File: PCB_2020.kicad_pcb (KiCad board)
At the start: 2 copper layers, 109.5 x 87.9 mm, 34 parts, among them Q1 100V/17A, Q2 100V/17A, Q3 100V/17A, Q4 100V/17A, Q5 100V/17A, Q6 100V/17A, U1 AMP_DUE_SCH, U2 TL084CN, U3 DRV8874, U4 LoRa

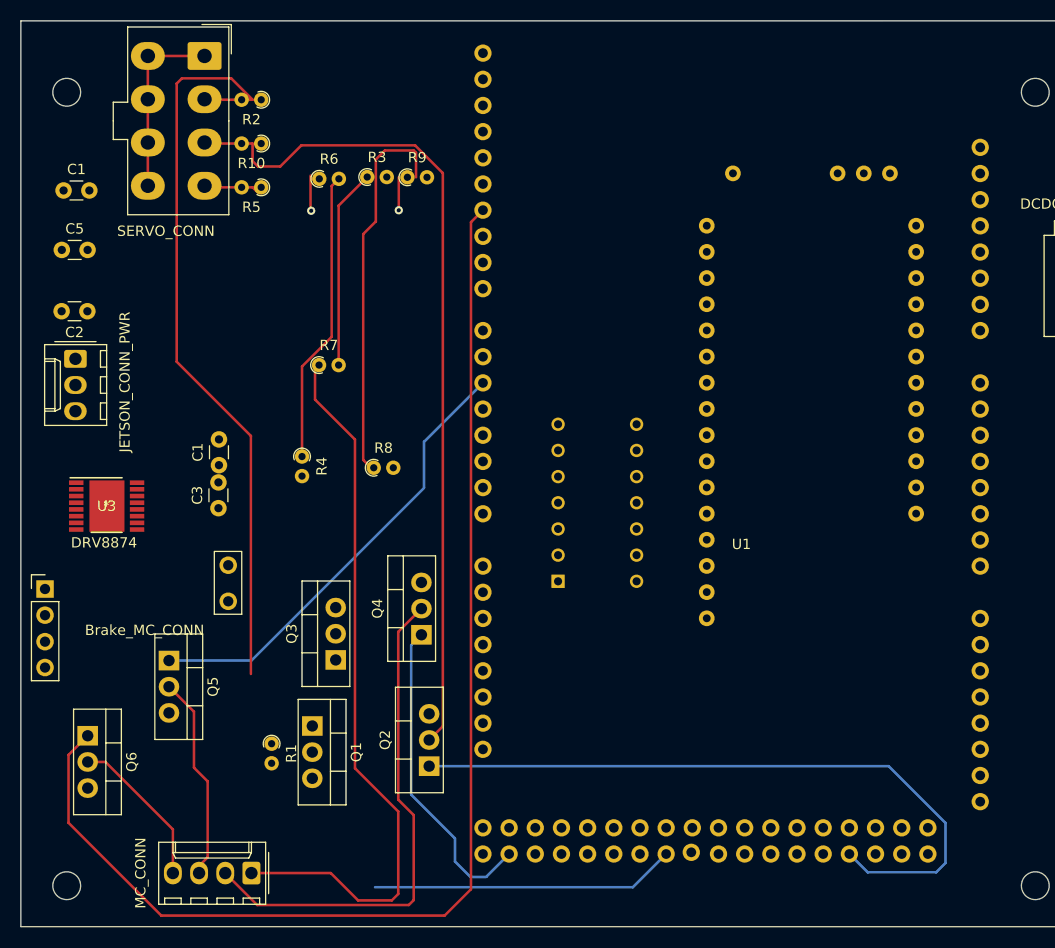
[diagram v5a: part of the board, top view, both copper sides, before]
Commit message: Added AND gate for Feather LoRa, and changed over to through hole components
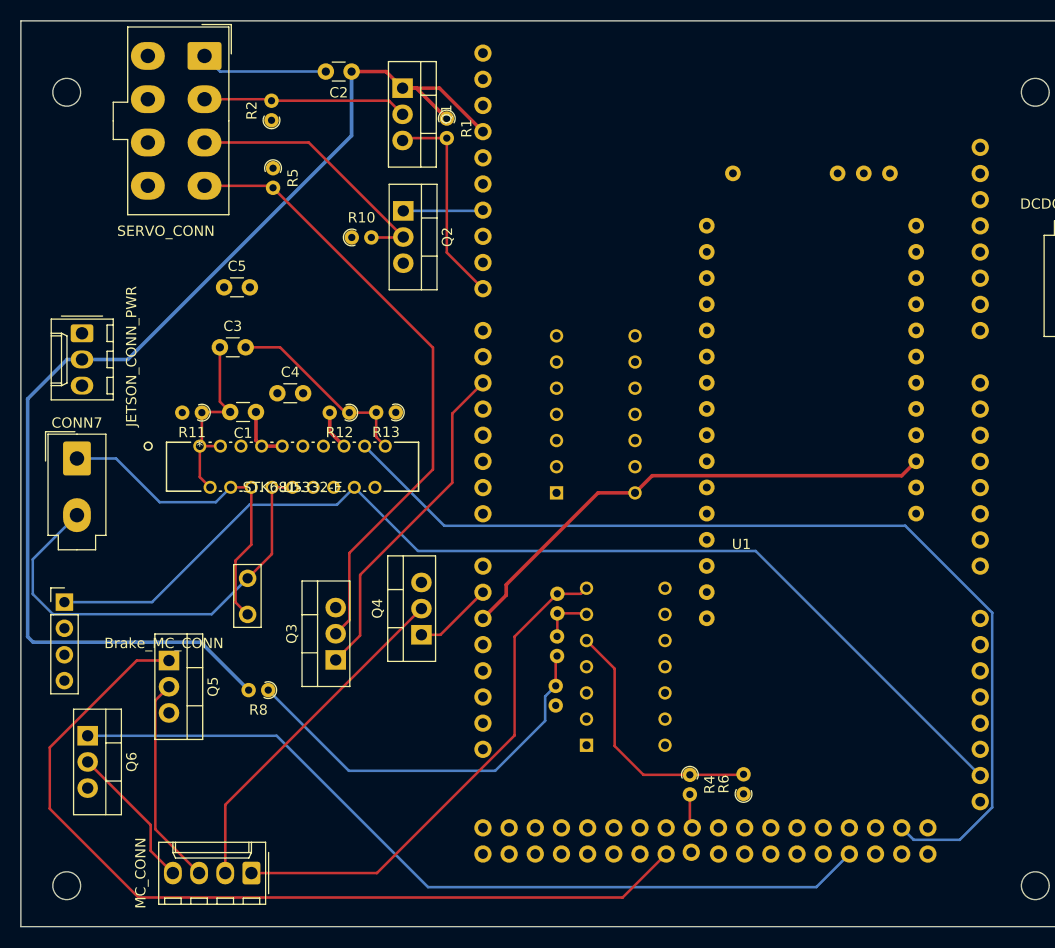
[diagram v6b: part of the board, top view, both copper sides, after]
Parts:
- removed the C1 at (131.0, 66.1)
- removed the C1 at (146.1, 92.8)
- added C1: 47u, Capacitor_THT:C_Disc_D3.0mm_W1.6mm_P2.50mm, F.Cu at (149.7, 87.6)
- added C4: 10u, Capacitor_THT:C_Disc_D3.0mm_W1.6mm_P2.50mm, F.Cu at (151.8, 85.8)
- added CONN7: Brake_CONN, Connector_Molex:Molex_Mini-Fit_Jr_5566-02A_2x01_P4.20mm_Vertical, F.Cu at (132.3, 92.1)
- added R11: R-Device, Resistor_THT:R_Axial_DIN0204_L3.6mm_D1.6mm_P1.90mm_Vertical, F.Cu at (144.4, 87.7)
- added R12: 4k, Resistor_THT:R_Axial_DIN0204_L3.6mm_D1.6mm_P1.90mm_Vertical, F.Cu at (158.8, 87.7)
- added R13: 1k, Resistor_THT:R_Axial_DIN0204_L3.6mm_D1.6mm_P1.90mm_Vertical, F.Cu at (163.3, 87.7)
- added U5: STK681-332-E, Drivetrain_control:STK681-332-E, F.Cu at (144.2, 90.9)
- C3: value 0.022uF -> 0.1u
- R3, R7, R9: moved to B.Cu
- U3: value DRV8874 -> SN74AS08N; footprint Drivetrain_control:DRV8874PWPR -> Drivetrain_control:SN74AS08N; moved to B.Cu
- moved R6 72.5 mm to (197.0, 124.7), turned to 90 degrees
- moved R1 63.0 mm to (168.2, 59.1)
- moved Q1 62.5 mm to (163.9, 56.2)
- moved Q2 53.9 mm to (164.0, 68.1), turned to 270 degrees
- moved U3 53.9 mm to (186.5, 80.2)
- moved R9 53.2 mm to (178.8, 116.1), turned to 90 degrees
- moved R4 48.7 mm to (191.8, 122.8)
- moved R3 48.2 mm to (178.9, 109.4), turned to 270 degrees
- moved C2 34.6 mm to (159.0, 54.6)
- moved R7 32.1 mm to (178.9, 105.3), turned to 270 degrees
- moved R8 23.9 mm to (150.9, 114.6), turned to 180 degrees
- moved C5 16.2 mm to (146.6, 75.5)
- moved U2 16.1 mm to (189.4, 104.7)
- moved C3 15.6 mm to (146.2, 81.3), turned to 0 degrees
- moved R10 12.7 mm to (159.0, 70.7), turned to 0 degrees
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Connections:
- C3 pad 1: +12V -> Net-(C1-Pad2)
- U1 pad 18: Brake_PWM_1 -> Net-(U1-Pad18)
- U1 pad 19: Brake_PWM_2 -> Net-(U1-Pad19)
- U1 pad 20: STEERING -> Net-(U1-Pad20)
- U1 pad 23: Net-(U1-Pad23) -> Brake_PWM_1
- U1 pad 26: Net-(U1-Pad26) -> Brake_PWM_2
- U1 pad 46: INPUT_A+_CTL -> FS1_CTL
- U1 pad 53: EN+_CTL -> FWD_CTL
- U1 pad 59: REV_CTL -> KS1_CTL
- U1 pad 67: KS1_CTL -> REV_CTL
- U1 pad 74: FWD_CTL -> EN+_CTL
- U1 pad 77: Net-(U1-Pad77) -> STEERING
- U1 pad 80: FS1_CTL -> INPUT_A+_CTL
- U3 pad 1: Brake_PWM_1 -> Net-(U3-Pad1)
- U3 pad 10: /LAUNCHXL-F28379D Breakout/Brake_Out_2 -> Net-(U3-Pad10)
- U3 pad 11: +12V -> Net-(U3-Pad11)
- U3 pad 12: Net-(C3-Pad2) -> Net-(U3-Pad12)
- U3 pad 14: Net-(C1-Pad2) -> +5V
- U3 pad 2: Brake_PWM_2 -> Net-(U3-Pad2)
- U3 pad 3: +3V3 -> Net-(U3-Pad3)
- U3 pad 5: +3V3 -> Net-(U3-Pad5)
- U3 pad 6: GND -> Net-(U3-Pad6)
- U3 pad 8: /LAUNCHXL-F28379D Breakout/Brake_Out_1 -> Net-(U3-Pad8)
- U3 pad 9: GND -> Net-(U3-Pad9)
- U4 pad 48: +3V3 -> Net-(U4-Pad48)
- U4 pad 55: Net-(U4-Pad55) -> +5V
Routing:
- net +3V3: track 0.00 -> 115.6 mm
- net Brake_PWM_1: track 0.00 -> 105.1 mm
- net Brake_PWM_2: track 0.00 -> 97.1 mm
- net INPUT_A+_CTL: track 66.7 -> 7.76 mm
- net /LAUNCHXL-F28379D Breakout/INPUT_A+: track 82.6 -> 26.2 mm
- net /LAUNCHXL-F28379D Breakout/EN+: track 5.56 -> 60.3 mm
- net /LAUNCHXL-F28379D Breakout/INPUT_B+: track 73.4 -> 19.8 mm
- net +5V: track 0.00 -> 52.8 mm
- net /LAUNCHXL-F28379D Breakout/Brake_Out_1: track 0.00 -> 44.3 mm
- net FWD_CTL: track 44.3 -> 86.1 mm
- net FS1_CTL: track 119.4 -> 81.3 mm
- net /LAUNCHXL-F28379D Breakout/Brake_Out_2: track 0.00 -> 32.7 mm
- net REV_CTL: track 31.0 -> 7.68 mm
- net /LAUNCHXL-F28379D Breakout/THROTTLE_MC: track 70.5 -> 49.6 mm
- net STEERING: track 0.00 -> 20.5 mm
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
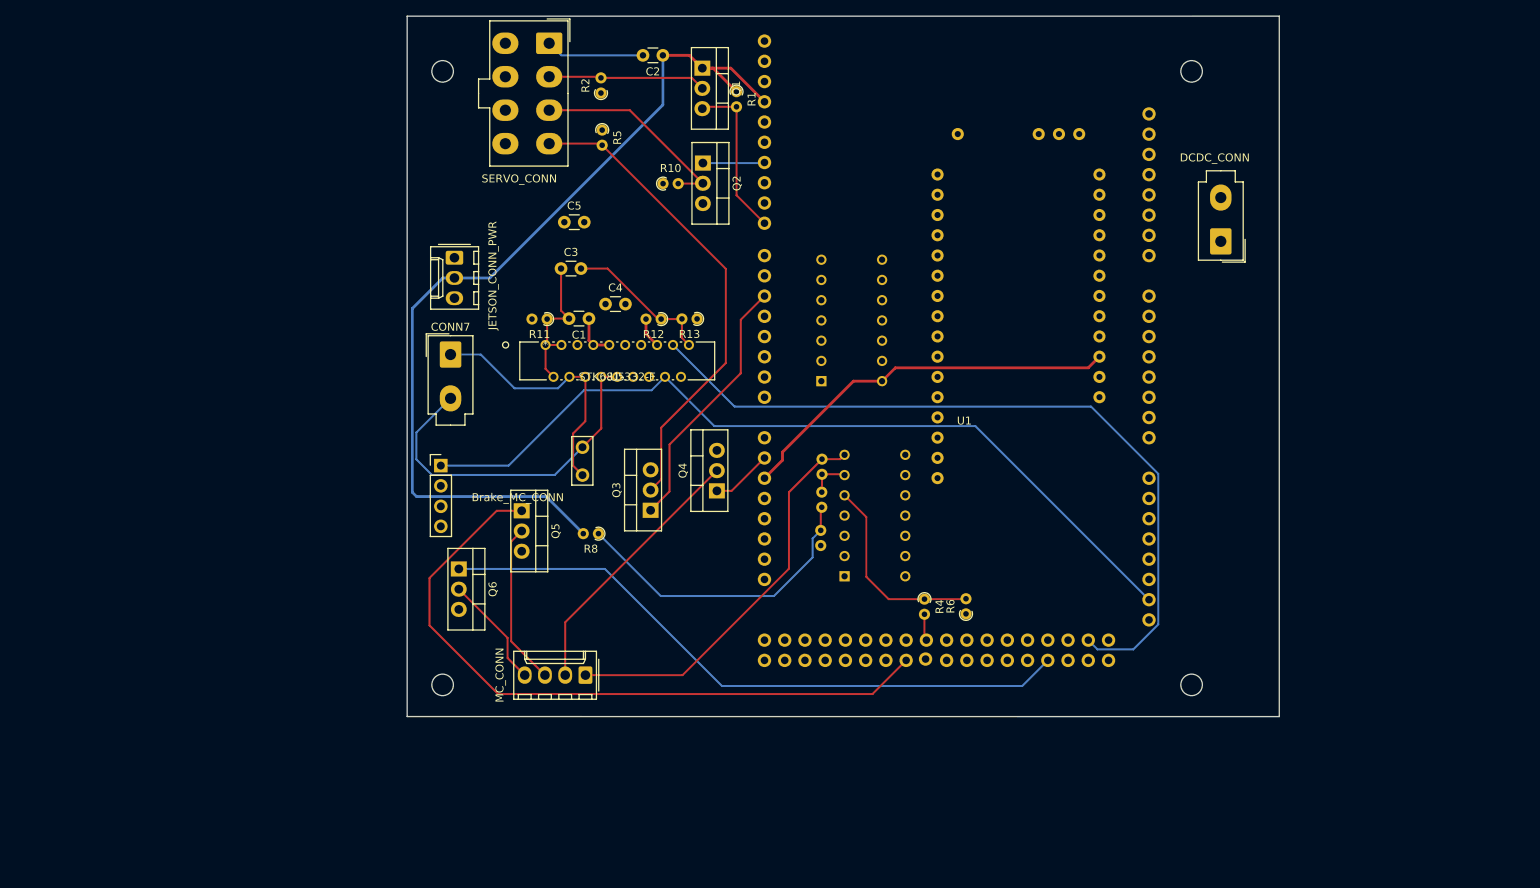
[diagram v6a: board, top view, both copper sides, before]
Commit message: updated PCB with bluetooth connector for arduino signals
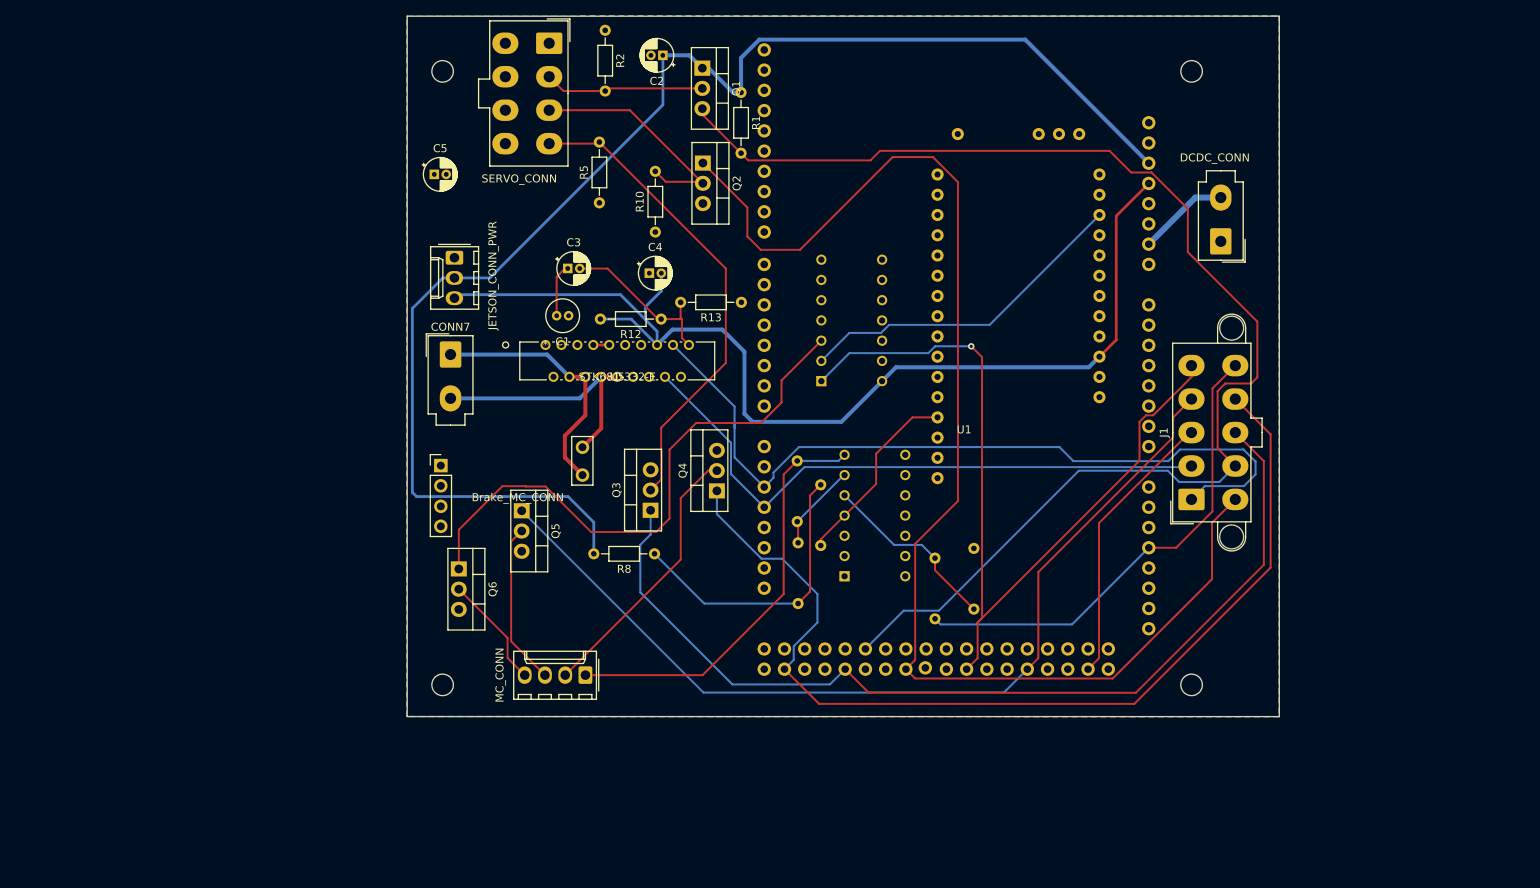
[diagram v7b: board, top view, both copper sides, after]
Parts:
- removed R11: R-Device, Resistor_THT:R_Axial_DIN0204_L3.6mm_D1.6mm_P1.90mm_Vertical
- added J1: Conn_01x10_Female, Connector_Molex:Molex_Mini-Fit_Jr_5566-10A2_2x05_P4.20mm_Vertical, F.Cu at (225.3, 110.3)
- C1: footprint Capacitor_THT:C_Disc_D3.0mm_W1.6mm_P2.50mm -> Capacitor_THT:C_Radial_D4.0mm_H5.0mm_P1.50mm
- C2, C3, C4, C5: footprint Capacitor_THT:C_Disc_D3.0mm_W1.6mm_P2.50mm -> Capacitor_THT:CP_Radial_D4.0mm_P1.50mm
- R1, R10, R12, R13, R2, R3, R5, R7, R8, R9: footprint Resistor_THT:R_Axial_DIN0204_L3.6mm_D1.6mm_P1.90mm_Vertical -> Resistor_THT:R_Axial_DIN0204_L3.6mm_D1.6mm_P7.62mm_Horizontal
- R4, R6: footprint Resistor_THT:R_Axial_DIN0204_L3.6mm_D1.6mm_P1.90mm_Vertical -> Resistor_THT:R_Axial_DIN0204_L3.6mm_D1.6mm_P7.62mm_Horizontal; moved to B.Cu
- moved C5 17.4 mm to (130.3, 69.5)
- moved R5 9.14 mm to (151.0, 73.1), turned to 90 degrees
- moved R6 8.28 mm to (198.0, 116.5), turned to 270 degrees
- moved R2 7.89 mm to (151.7, 51.5), turned to 270 degrees
- moved R8 7.48 mm to (157.9, 117.2)
- moved R3 7.02 mm to (175.9, 115.8)
- moved C4 6.73 mm to (157.3, 81.9)
- moved R10 6.16 mm to (158.0, 76.8), turned to 90 degrees
- moved R13 5.94 mm to (168.8, 85.6)
- moved R4 5.32 mm to (193.1, 117.7)
- moved R7 3.12 mm to (175.8, 105.5)
- moved C1 2.58 mm to (147.1, 87.3)
- moved U1 1.11 mm to (196.1, 100.8)
- moved C3 0.84 mm to (147.0, 81.3)
- moved R1 0.58 mm to (168.8, 59.2)
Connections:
- C1 pad 2: Net-(C1-Pad2) -> GND
- C3 pad 1: Net-(C1-Pad2) -> GND
- Q6 pad 1: FS1_CTL -> FS1_RMT
- U1 pad 20: Net-(U1-Pad20) -> THROTTLE
- U1 pad 23: Brake_PWM_1 -> Net-(U1-Pad23)
- U1 pad 24: +12V -> Net-(U1-Pad24)
- U1 pad 26: Brake_PWM_2 -> Net-(U1-Pad26)
- U1 pad 28: SCIB_TX -> Net-(U1-Pad28)
- U1 pad 3: Net-(U1-Pad3) -> +3V3
- U1 pad 34: THROTTLE -> Net-(U1-Pad34)
- U1 pad 36: SCIB_RX -> Net-(U1-Pad36)
- U1 pad 37: Net-(U1-Pad37) -> STEERING
- U1 pad 4: Net-(U1-Pad4) -> +5V
- U1 pad 41: GND -> Net-(U1-Pad41)
- U1 pad 42: GND -> Net-(U1-Pad42)
- U1 pad 44: Net-(U1-Pad44) -> KS1_CTL
- U1 pad 46: FS1_CTL -> Net-(U1-Pad46)
- U1 pad 47: Net-(U1-Pad47) -> FWD_CTL
- U1 pad 5: Net-(U1-Pad5) -> GND
- U1 pad 50: Net-(U1-Pad50) -> FS1_CTL
- U1 pad 53: FWD_CTL -> INPUT_A+_CTL
- U1 pad 56: Net-(U1-Pad56) -> EN+_CTL
- U1 pad 59: KS1_CTL -> REV_CTL
- U1 pad 6: Net-(U1-Pad6) -> GND
- U1 pad 65: Net-(U1-Pad65) -> Brake_PWM_1
- U1 pad 66: +5V -> Brake_PWM_2
- U1 pad 67: REV_CTL -> Net-(U1-Pad67)
- U1 pad 69: Net-(U1-Pad69) -> SCIB_RX
- U1 pad 7: Net-(U1-Pad7) -> +12V
- U1 pad 70: Net-(U1-Pad70) -> SCIB_TX
- U1 pad 74: EN+_CTL -> Net-(U1-Pad74)
- U1 pad 77: STEERING -> Net-(U1-Pad77)
- U1 pad 80: INPUT_A+_CTL -> Net-(U1-Pad80)
- U1 pad 83: +3V3 -> Net-(U1-Pad83)
- U1 pad 86: (no net) -> Net-(U1-Pad86)
- U3 pad 1: Net-(U3-Pad1) -> FS1_CTL
- U3 pad 3: Net-(U3-Pad3) -> FS1_RMT
- U4 pad 24: Net-(U4-Pad24) -> Net-(U3-Pad2)
- U5 pad 1: Net-(C1-Pad2) -> GND
- U5 pad 2: Net-(C1-Pad2) -> GND
- U5 pad 3: Net-(C1-Pad2) -> GND
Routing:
- net INPUT_A+_CTL: track 7.76 -> 163.9 mm
- net STEERING: track 20.5 -> 165.4 mm
- net REV_CTL: track 7.68 -> 123.7 mm
- net EN+_CTL: track 32.8 -> 120.6 mm
- net +5V: track 52.8 -> 137.7 mm
- net FS1_RMT: track 0.00 -> 71.7 mm
- net +3V3: track 115.6 -> 174.2 mm
- net THROTTLE: track 3.34 -> 60.5 mm
- net Net-(U3-Pad2): track 0.00 -> 42.5 mm
- net KS1_CTL: track 0.00 -> 35.2 mm
- net FWD_CTL: track 86.1 -> 116.6 mm
- net Brake_PWM_1: track 105.1 -> 77.3 mm
- net FS1_CTL: track 81.3 -> 106.4 mm, vias 0 -> 1
- net Net-(C1-Pad2): track 19.2 -> 0.00 mm
- net GND: track 12.4 -> 31.0 mm
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- added copper zone on F.Cu, net +12V
- added copper zone on B.Cu, net GND
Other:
- net class Power: trace_width 0.35 -> 0.5
